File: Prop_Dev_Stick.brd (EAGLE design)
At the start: 63.2 x 24.4 mm, 52 parts, among them J1 10118193-0001LF, J3 M20-7822046, J4 M20-7822046, J5 M20-7820442, J6 M20-7820442, U1 P8X32A-Q44, U2 FT230XQ-R, U4 CAT24C512WI-GT3, U5 AD7999YRJZ-1500RL7, U6 TS2937CW33, U7 IRLML6401TRPBF, U8 TPS2115ADRBR, X1 ATS060CSM-1

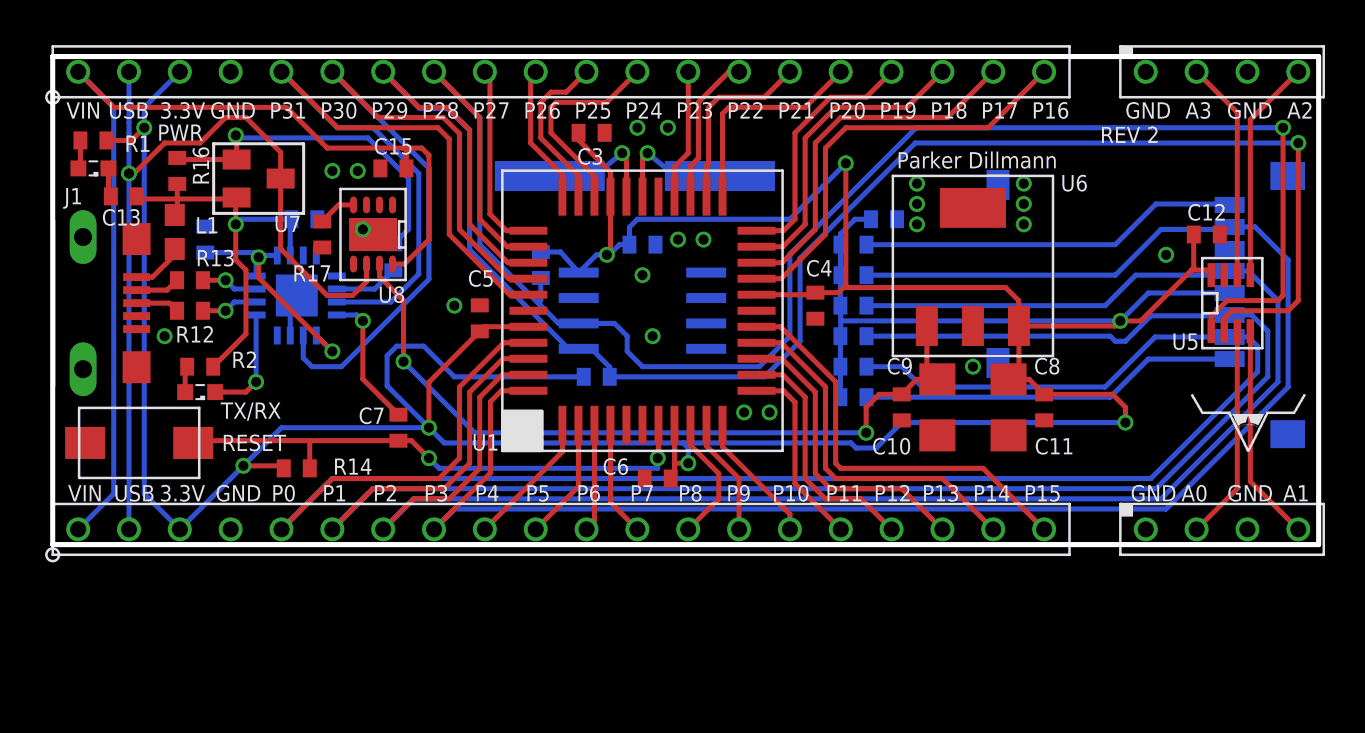
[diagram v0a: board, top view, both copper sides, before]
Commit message: Adjusted edge of board to remove DRC issues.
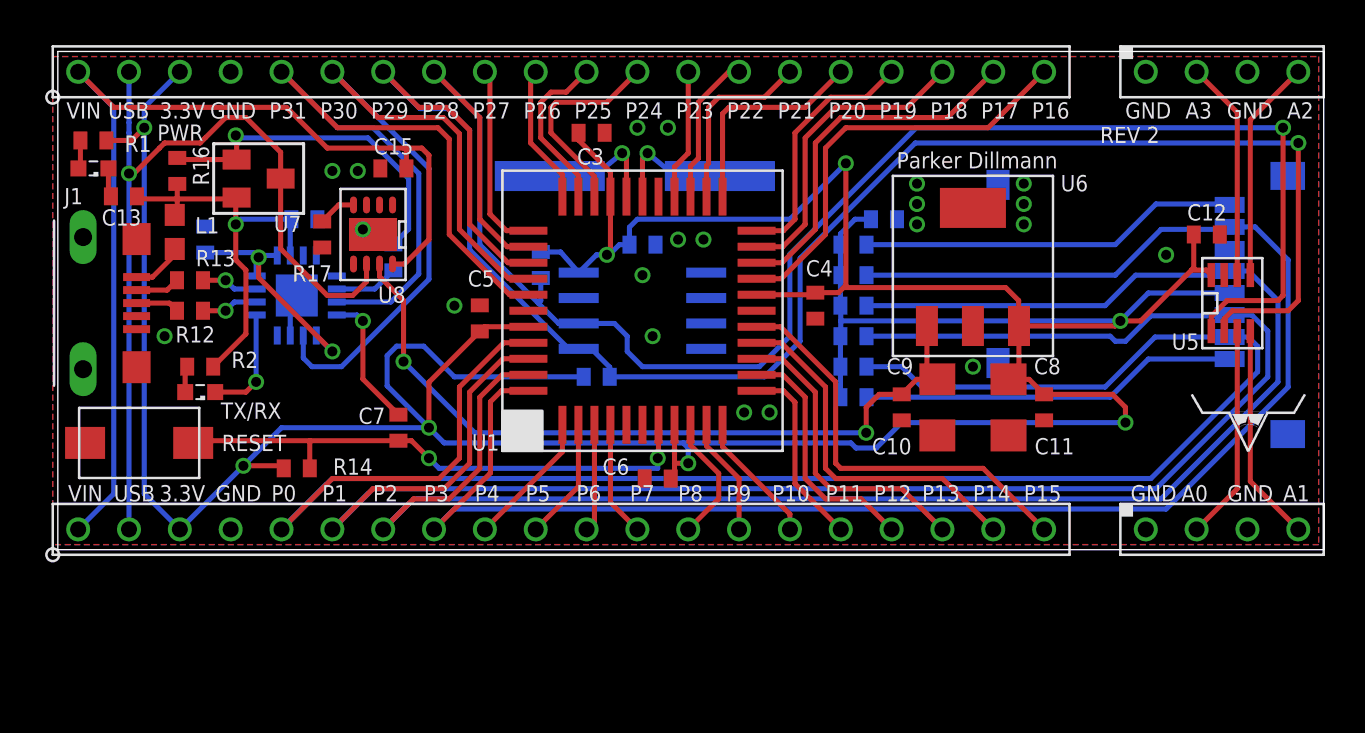
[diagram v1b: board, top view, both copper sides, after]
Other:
- board size 63.2 x 24.4 mm -> 63.2 x 24.9 mm
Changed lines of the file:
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@@
 <?xml version="1.0" encoding="utf-8"?>
 <!DOCTYPE eagle SYSTEM "eagle.dtd">
-<eagle version="6.3">
+<eagle version="6.5.0">
 <drawing>
 <settings>
@@
 <board>
 <plain>
-<wire x1="0" y1="24.384" x2="63.246" y2="24.384" width="0.254" layer="20"/>
-<wire x1="63.246" y1="24.384" x2="63.246" y2="0" width="0.254" layer="20"/>
-<wire x1="63.246" y1="0" x2="0" y2="0" width="0.254" layer="20"/>
-<wire x1="0" y1="0" x2="0" y2="24.384" width="0.254" layer="20"/>
+<wire x1="0.254" y1="24.638" x2="63.5" y2="24.638" width="0" layer="20"/>
+<wire x1="63.5" y1="24.638" x2="63.5" y2="-0.254" width="0" layer="20"/>
+<wire x1="63.5" y1="-0.254" x2="0.254" y2="-0.254" width="0" layer="20"/>
+<wire x1="0.254" y1="-0.254" x2="0.254" y2="24.638" width="0" layer="20"/>
 <text x="3.048" y="2.159" size="0.8128" layer="21" font="vector">USB</text>
 <text x="5.334" y="2.159" size="0.8128" layer="21" font="vector">3.3V</text>

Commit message: Finished REV3!!!
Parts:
- removed U8: TPS2115ADRBR, PP_PowerIC:SON-8
- added U3: TPS2111APWR, PP_PowerIC:SON-8
- C1, C10, C11, C12, C13, C14, C15, C16, C2, C3, C4, C5, C6, C7, R1, R10, R11, R12, R13, R14, R15, R16, R17, R2, R4, R5, R6, R7, R8, R9: device PP_Passives:0402 -> PP_Passives:0603
- PWR: value 598-8070-107F -> 598-8020-107F; device led:SML0603 -> PP_LED:LED_0805
- TX/RX: device led:SML0603 -> PP_LED:LED_0805
- moved C12 34.1 mm to (23.6, 14.2), flipped to the bottom, turned to 90 degrees
- moved C14 28.9 mm to (58.2, 11.7), turned to 270 degrees
- moved U$2 23.0 mm to (42.2, 16.8)
- moved R1 18.3 mm to (11.4, 4.45)
- moved PWR 15.5 mm to (7.62, 4.32), turned to 0 degrees
- moved RESET 15.0 mm to (18.3, 10.7), turned to 270 degrees
- moved C11 13.5 mm to (48.0, 20.3), flipped to the bottom, turned to 0 degrees
- moved C10 13.5 mm to (43.4, 20.3), flipped to the bottom, turned to 180 degrees
- moved C9 11.5 mm to (42.7, 18.3), flipped to the bottom, turned to 180 degrees
- moved C8 11.5 mm to (48.8, 18.3), flipped to the bottom, turned to 0 degrees
- moved C16 10.7 mm to (42.3, 5.59), flipped to the top, turned to 0 degrees
- moved C13 9.23 mm to (12.7, 16.1), flipped to the bottom
- moved R11 8.75 mm to (43.8, 7.11), flipped to the top, turned to 180 degrees
- moved R6 8.29 mm to (43.8, 14.7), flipped to the top, turned to 180 degrees
- moved R10 6.15 mm to (43.8, 8.64), flipped to the top, turned to 180 degrees
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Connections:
- net 3.3V: now also J5.2, J6.2
- net 3V3OUT: now also R2.2
- net 5V: now also U3.7; no longer U8.7
- net A0: now also J6.4; no longer J6.2
- net A1: now also J6.3; no longer J6.4
- net A2: now also J5.3; no longer J5.4
- net A3: now also J5.4; no longer J5.2
- net GND: now also PWR.CATHODE, U3.2, U3.5; no longer J5.3, J6.3, PWR.C, U8.3, U8.5, U8.PAD
- net N$1: now also PWR.ANODE; no longer PWR.A
- net N$2: now also TX/RX.ANODE; no longer TX/RX.A
- net N$7: now also U3.4; no longer U8.4
- net TX_RX_LED: now also TX/RX.CATHODE; no longer TX/RX.C
- net VBUS: now also L1.1; no longer L1.2
- net VBUS_P1: now also L1.2; no longer L1.1, R2.2
- net VBUS_P2: now also U3.6; no longer U8.6
- net VIN: now also U3.3, U3.8; no longer U8.8
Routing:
- net SDA: track 89.6 -> 69.9 mm, vias 1 -> 3
- net SD_DO: track 84.4 -> 66.2 mm, vias 0 -> 1
- net SCL: track 85.8 -> 68.9 mm, vias 1 -> 3
- net SD_SCLK: track 88.0 -> 71.8 mm, vias 0 -> 1
- net SD_DI: track 91.1 -> 78.1 mm, vias 0 -> 1
- net SD_CS: track 96.0 -> 83.9 mm, vias 0 -> 1
- net TX: track 38.4 -> 27.2 mm, vias 0 -> 1
- net RX: track 38.6 -> 30.0 mm, vias 0 -> 1
- net VBUS_P1: track 20.7 -> 13.0 mm
- net VBUS_P2: track 43.8 -> 51.3 mm
- net RES: track 27.4 -> 22.8 mm
- net IRQ: track 19.0 -> 14.5 mm
- net 3V3OUT: track 12.1 -> 16.0 mm
- net RW: track 18.9 -> 15.0 mm
- net X0: track 6.29 -> 9.82 mm
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
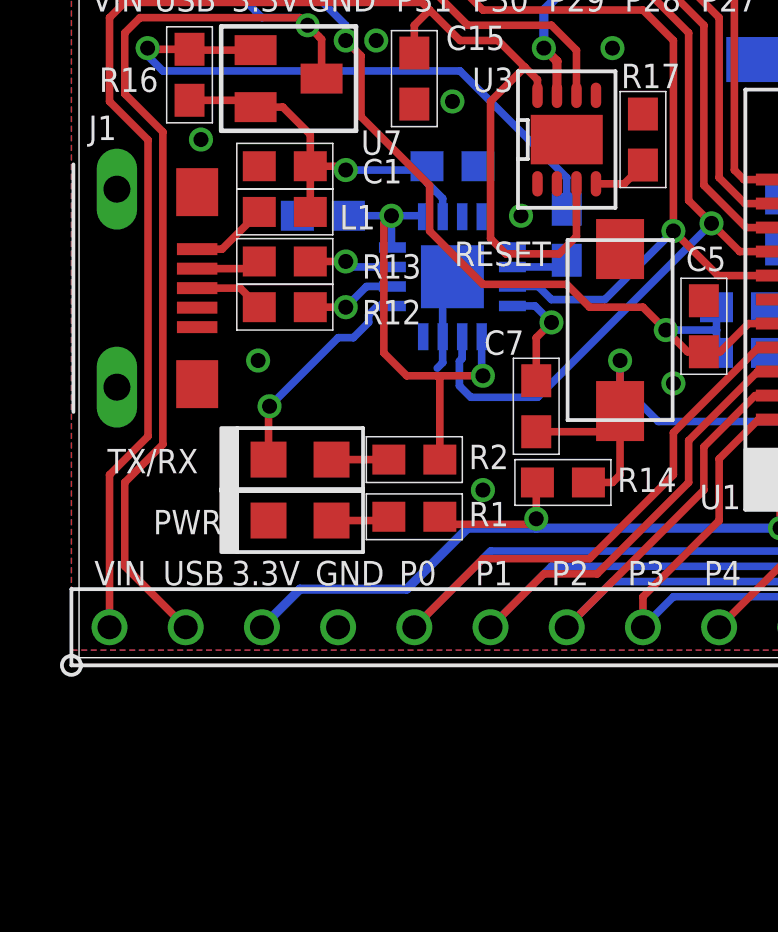
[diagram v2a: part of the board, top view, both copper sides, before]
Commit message: Added power switching for LDO Voltage Dropout.
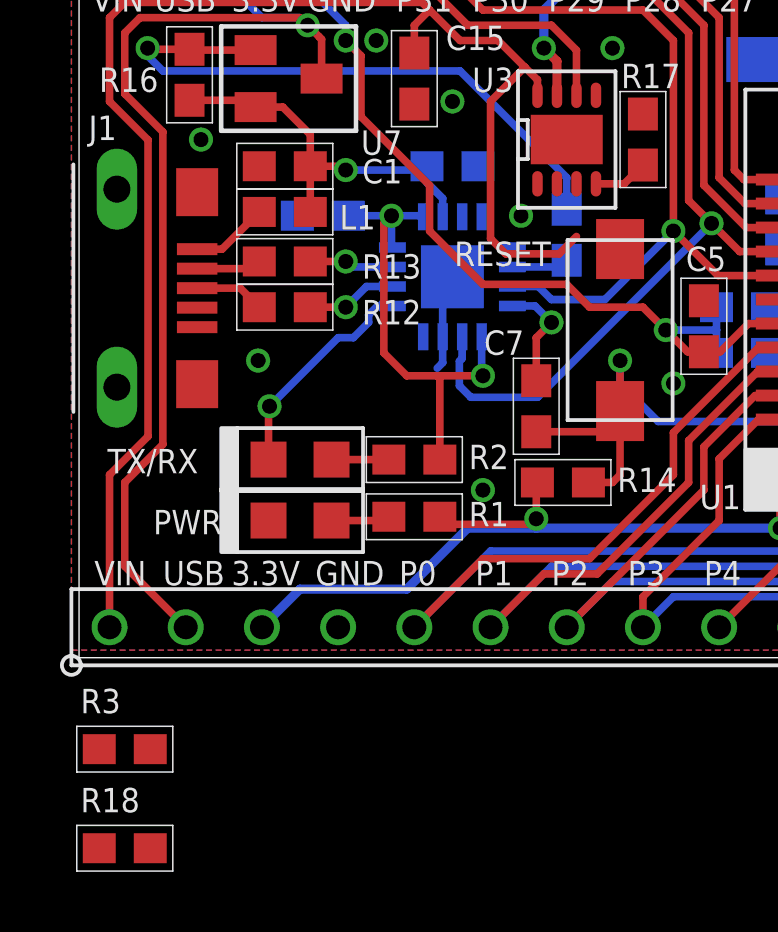
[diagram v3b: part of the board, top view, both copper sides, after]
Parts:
- added R18: 25K, PP_Passives:0603
- added R3: 100K, PP_Passives:0603
- C13: value .1uF -> 1uF
- U3: value TPS2111APWR -> TPS2113ADRBR
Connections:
- new net VSNS: R18.2, R3.1, U3.3
- net GND: now also R18.1
- net VIN: now also R3.2; no longer U3.3
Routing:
- net VIN: track 52.6 -> 50.8 mm
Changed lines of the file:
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@@
 </element>
 <element name="U$1" library="PP_Aesthetics" package="LHE_FRAME" value="LHE_FRAME" x="39.116" y="1.016" smashed="yes" rot="MR0">
-<attribute name="REVNUM" value="REV 3" x="62.992" y="17.526" size="0.8128" layer="22" font="vector" rot="MR0"/>
+<attribute name="REVNUM" value="REV 4" x="62.992" y="17.526" size="0.8128" layer="22" font="vector" rot="MR0"/>
 <attribute name="PNAME" value="Propeller Dev Stick" x="39.116" y="3.556" size="0.8128" layer="22" font="vector" rot="MR0" display="off"/>
 <attribute name="DNAME" value="Parker Dillmann" x="62.992" y="20.066" size="0.8128" layer="22" font="vector" rot="MR0"/>
@@
 <attribute name="NAME" x="0.924" y="18.6055" size="0.8128" layer="25" font="vector"/>
 </element>
-<element name="C13" library="PP_Passives" package="0603" value=".1uF" x="12.7" y="16.129" smashed="yes" rot="MR180">
+<element name="C13" library="PP_Passives" package="0603" value="1uF" x="12.7" y="16.129" smashed="yes" rot="MR180">
 <attribute name="NAME" x="11.592" y="17.8435" size="0.8128" layer="26" font="vector" rot="MR180"/>
 </element>
@@
 <attribute name="NAME" x="2.726" y="3.861" size="0.8128" layer="25" font="vector"/>
 </element>
-<element name="U3" library="PP_PowerIC" package="SON-8" value="TPS2111APWR" x="16.51" y="17.018" smashed="yes">
+<element name="U3" library="PP_PowerIC" package="SON-8" value="TPS2113ADRBR" x="16.51" y="17.018" smashed="yes">
 <attribute name="NAME" x="13.361" y="18.602" size="0.8128" layer="21" font="vector"/>
 </element>
+<element name="R3" library="PP_Passives" package="0603" value="100K" x="1.778" y="-3.302"/>
+<element name="R18" library="PP_Passives" package="0603" value="25K" x="1.778" y="-6.604"/>
 </elements>
 <signals>
@@
 <via x="20.066" y="8.89" extent="1-16" drill="0.5"/>
 <via x="6.223" y="9.652" extent="1-16" drill="0.5"/>
+<contactref element="R18" pad="1"/>
+<wire x1="47.156" y1="20.32" x2="54.61" y2="23.622" width="0" layer="19" extent="16-16"/>
+<wire x1="47.368" y1="18.288" x2="47.156" y2="20.32" width="0" layer="19" extent="16-16"/>
+<wire x1="44.284" y1="20.32" x2="47.156" y2="20.32" width="0" layer="19" extent="16-16"/>
+<wire x1="44.072" y1="18.288" x2="44.284" y2="20.32" width="0" layer="19" extent="16-16"/>
+<wire x1="45.72" y1="15.494" x2="47.368" y2="18.288" width="0" layer="19" extent="16-16"/>
+<wire x1="47.226" y1="15.059" x2="45.72" y2="15.494" width="0" layer="19" extent="1-16"/>
+<wire x1="57.404" y1="9.144" x2="58.801" y2="9.359" width="0" layer="19" extent="1-1"/>
+<wire x1="58.166" y1="10.834" x2="58.801" y2="9.359" width="0" layer="19" extent="1-16"/>
+<wire x1="48.768" y1="5.588" x2="47.226" y2="6.159" width="0" layer="19" extent="1-1"/>
+<wire x1="44.958" y1="5.588" x2="47.226" y2="6.159" width="0" layer="19" extent="1-1"/>
+<wire x1="43.141" y1="5.588" x2="44.958" y2="5.588" width="0" layer="19" extent="1-1"/>
+<wire x1="45.72" y1="9.594" x2="47.226" y2="6.159" width="0" layer="19" extent="1-16"/>
+<wire x1="62.23" y1="14.732" x2="61.701" y2="18.609" width="0" layer="19" extent="1-1"/>
+<wire x1="61.864" y1="12.957" x2="62.23" y2="14.732" width="0" layer="19" extent="16-16"/>
+<wire x1="37.084" y1="20.574" x2="44.284" y2="20.32" width="0" layer="19" extent="16-16"/>
+<wire x1="30.06" y1="20.066" x2="37.084" y2="20.574" width="0" layer="19" extent="1-1"/>
+<wire x1="30.264" y1="17.384" x2="30.06" y2="20.066" width="0" layer="19" extent="1-1"/>
+<wire x1="32.649" y1="13.081" x2="30.988" y2="14.732" width="0" layer="19" extent="16-16"/>
+<wire x1="32.649" y1="11.811" x2="32.649" y2="13.081" width="0" layer="19" extent="16-16"/>
+<wire x1="32.649" y1="10.541" x2="32.649" y2="11.811" width="0" layer="19" extent="16-16"/>
+<wire x1="35.164" y1="11.684" x2="32.649" y2="11.811" width="0" layer="19" extent="1-16"/>
+<wire x1="32.893" y1="7.747" x2="32.649" y2="10.541" width="0" layer="19" extent="16-16"/>
+<wire x1="38.1" y1="11.088" x2="35.164" y2="11.684" width="0" layer="19" extent="1-1"/>
+<wire x1="29.464" y1="5.984" x2="32.893" y2="7.747" width="0" layer="19" extent="1-1"/>
+<wire x1="28.664" y1="5.984" x2="29.464" y2="5.984" width="0" layer="19" extent="1-1"/>
+<wire x1="29.376" y1="3.81" x2="29.464" y2="5.984" width="0" layer="19" extent="1-1"/>
+<wire x1="26.279" y1="13.081" x2="30.988" y2="14.732" width="0" layer="19" extent="16-16"/>
+<wire x1="23.622" y1="13.374" x2="26.279" y2="13.081" width="0" layer="19" extent="16-16"/>
+<wire x1="23.764" y1="11.684" x2="23.622" y2="13.374" width="0" layer="19" extent="1-16"/>
+<wire x1="21.082" y1="11.645" x2="23.764" y2="11.684" width="0" layer="19" extent="1-1"/>
+<wire x1="20.066" y1="8.89" x2="21.082" y2="11.645" width="0" layer="19" extent="1-1"/>
+<wire x1="18.288" y1="13.368" x2="21.082" y2="11.645" width="0" layer="19" extent="1-1"/>
+<wire x1="16.185" y1="15.543" x2="18.288" y2="13.368" width="0" layer="19" extent="1-1"/>
+<wire x1="14.986" y1="14.478" x2="16.185" y2="15.543" width="0" layer="19" extent="1-1"/>
+<wire x1="14.7" y1="13.421" x2="14.986" y2="14.478" width="0" layer="19" extent="16-16"/>
+<wire x1="13.55" y1="16.129" x2="14.986" y2="14.478" width="0" layer="19" extent="16-16"/>
+<wire x1="12.7" y1="12.446" x2="14.7" y2="13.421" width="0" layer="19" extent="16-16"/>
+<wire x1="12.7" y1="18.288" x2="13.55" y2="16.129" width="0" layer="19" extent="16-16"/>
+<wire x1="11.43" y1="18.2" x2="12.7" y2="18.288" width="0" layer="19" extent="1-1"/>
+<wire x1="10.16" y1="20.32" x2="11.43" y2="18.2" width="0" layer="19" extent="1-1"/>
+<wire x1="17.485" y1="18.493" x2="16.185" y2="15.543" width="0" layer="19" extent="1-1"/>
+<wire x1="19.05" y1="17.868" x2="17.485" y2="18.493" width="0" layer="19" extent="1-1"/>
+<wire x1="18.034" y1="20.066" x2="17.485" y2="18.493" width="0" layer="19" extent="1-1"/>
+<wire x1="8.89" y1="23.622" x2="10.16" y2="20.32" width="0" layer="19" extent="1-1"/>
+<wire x1="13.716" y1="5.334" x2="12.192" y2="9.398" width="0" layer="19" extent="16-16"/>
+<wire x1="7.532" y1="14.478" x2="12.375" y2="12.121" width="0" layer="19" extent="16-16"/>
+<wire x1="6.262" y1="16.129" x2="7.532" y2="14.478" width="0" layer="19" extent="1-16"/>
+<wire x1="4.318" y1="17.018" x2="6.262" y2="16.129" width="0" layer="19" extent="1-1"/>
+<wire x1="4.191" y1="15.265" x2="4.318" y2="17.018" width="0" layer="19" extent="1-1"/>
+<wire x1="1.516" y1="15.365" x2="4.191" y2="15.265" width="0" layer="19" extent="1-1"/>
+<wire x1="4.191" y1="10.765" x2="4.191" y2="15.265" width="0" layer="19" extent="1-1"/>
+<wire x1="4.191" y1="8.865" x2="4.191" y2="10.765" width="0" layer="19" extent="1-1"/>
+<wire x1="6.223" y1="9.652" x2="4.191" y2="8.865" width="0" layer="19" extent="1-1"/>
+<wire x1="1.516" y1="8.765" x2="4.191" y2="8.865" width="0" layer="19" extent="1-1"/>
+<wire x1="6.57" y1="4.318" x2="4.191" y2="8.865" width="0" layer="19" extent="1-1"/>
+<wire x1="8.89" y1="0.762" x2="6.57" y2="4.318" width="0" layer="19" extent="1-1"/>
+<wire x1="54.61" y1="0.762" x2="48.768" y2="5.588" width="0" layer="19" extent="1-1"/>
+<wire x1="0.928" y1="-6.604" x2="8.89" y2="0.762" width="0" layer="19" extent="1-1"/>
 </signal>
 <signal name="SDA">
@@
 <contactref element="J4" pad="1"/>
 <contactref element="C15" pad="2"/>
-<contactref element="U3" pad="3"/>
 <contactref element="U3" pad="8"/>
 <wire x1="11.684" y1="21.59" x2="11.938" y2="21.336" width="0.254" layer="1"/>
@@
 <wire x1="1.27" y1="21.082" x2="1.27" y2="18.288" width="0.254" layer="1"/>
 <wire x1="11.684" y1="21.59" x2="1.778" y2="21.59" width="0.254" layer="1"/>
-<wire x1="16.835" y1="15.543" x2="16.835" y2="13.787" width="0.254" layer="1"/>
 <wire x1="16.835" y1="13.787" x2="16.256" y2="13.208" width="0.254" layer="1"/>
 <wire x1="16.256" y1="13.208" x2="14.478" y2="13.208" width="0.254" layer="1"/>
@@
 <wire x1="11.43" y1="19.9" x2="11.43" y2="20.828" width="0.254" layer="1"/>
 <wire x1="11.43" y1="20.828" x2="11.938" y2="21.336" width="0.254" layer="1"/>
+<contactref element="R3" pad="2"/>
+<wire x1="2.628" y1="-3.302" x2="1.27" y2="0.762" width="0" layer="19" extent="1-1"/>
 </signal>
 <signal name="TX_RX_LED">
@@
 <wire x1="10.201" y1="11.471" x2="10.7" y2="11.471" width="0.254" layer="16"/>
 </signal>
+<signal name="VSNS">
+<contactref element="U3" pad="3"/>
+<contactref element="R3" pad="1"/>
+<contactref element="R18" pad="2"/>
+<wire x1="0.928" y1="-3.302" x2="16.835" y2="15.543" width="0" layer="19" extent="1-1"/>
+<wire x1="2.628" y1="-6.604" x2="0.928" y2="-3.302" width="0" layer="19" extent="1-1"/>
+</signal>
 </signals>
